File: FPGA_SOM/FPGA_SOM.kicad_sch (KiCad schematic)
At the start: 88 parts, among them J1 Conn_01x02, J1 USB_C_Receptacle_USB2.0, J3 Conn_02x06_Top_Bottom, J4 Conn_02x04_Counter_Clockwise, J5 Conn_01x06, J6 Conn_01x06, SW1 SW_Push, SW2 SW_Push, SW3 SW_Push, U101 W25Q128JVSIQ, U2 ICE40UP5K-SG48ITR, U3 AP2127N-3.3, U4 AP2127N-1.2, X101 SX2M36.000B10F20TNN

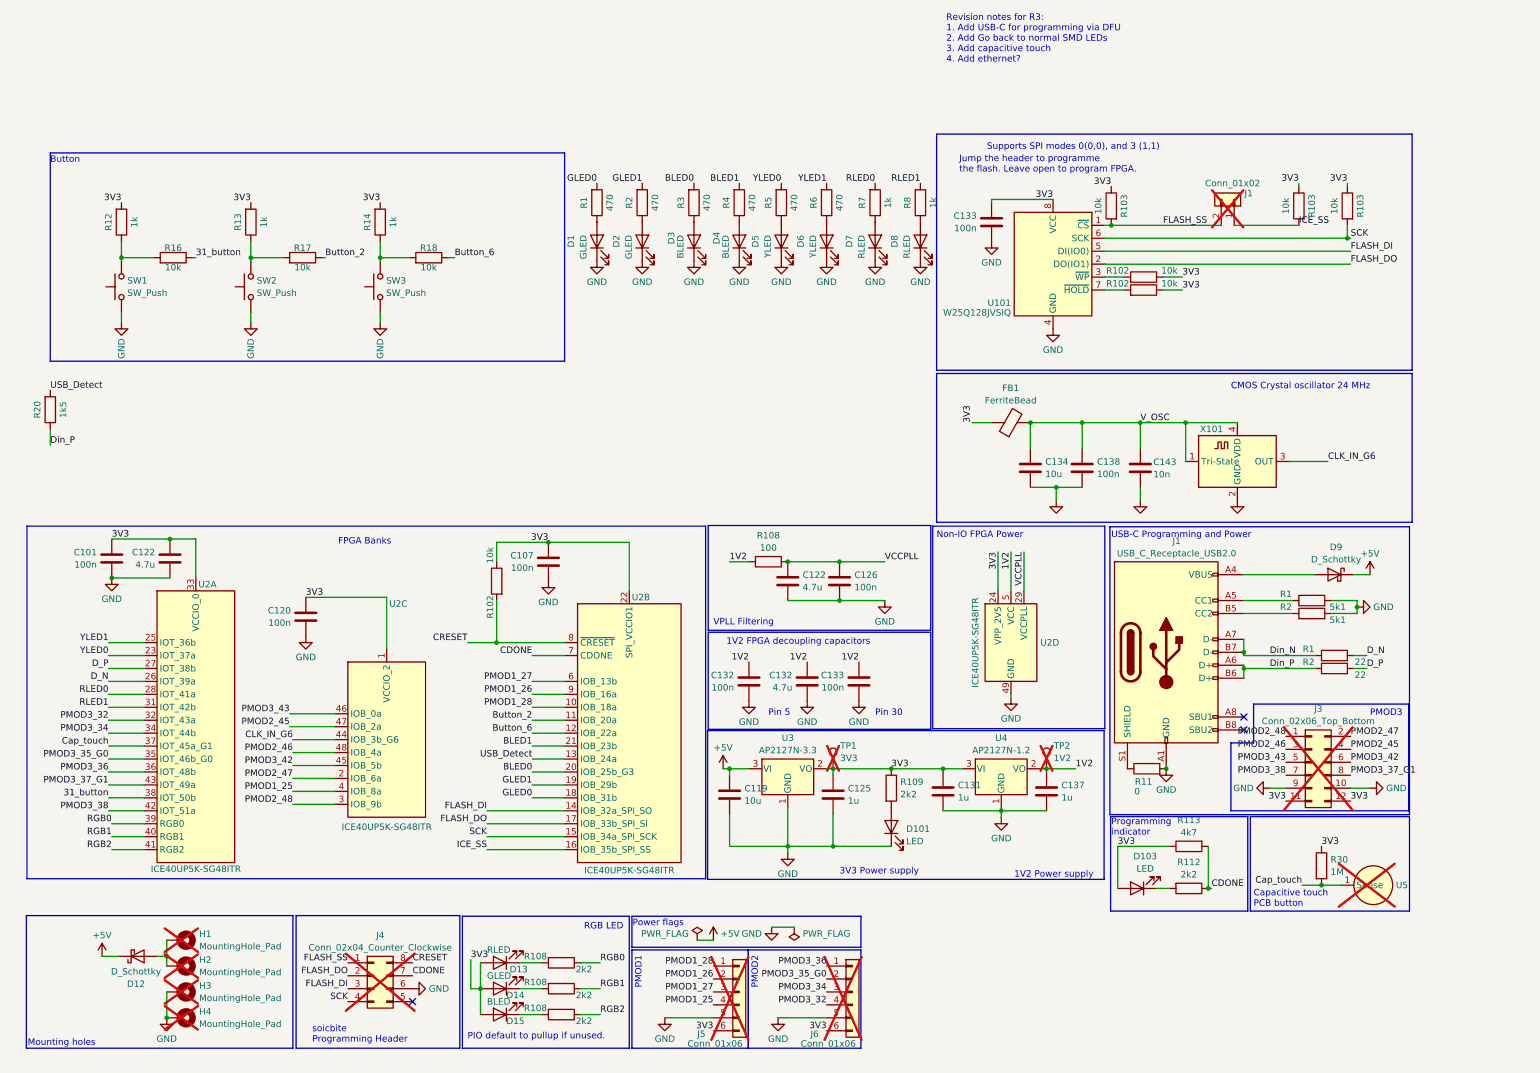
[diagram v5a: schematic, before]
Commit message: Kicad Update changes some things. Also reorganise nets.
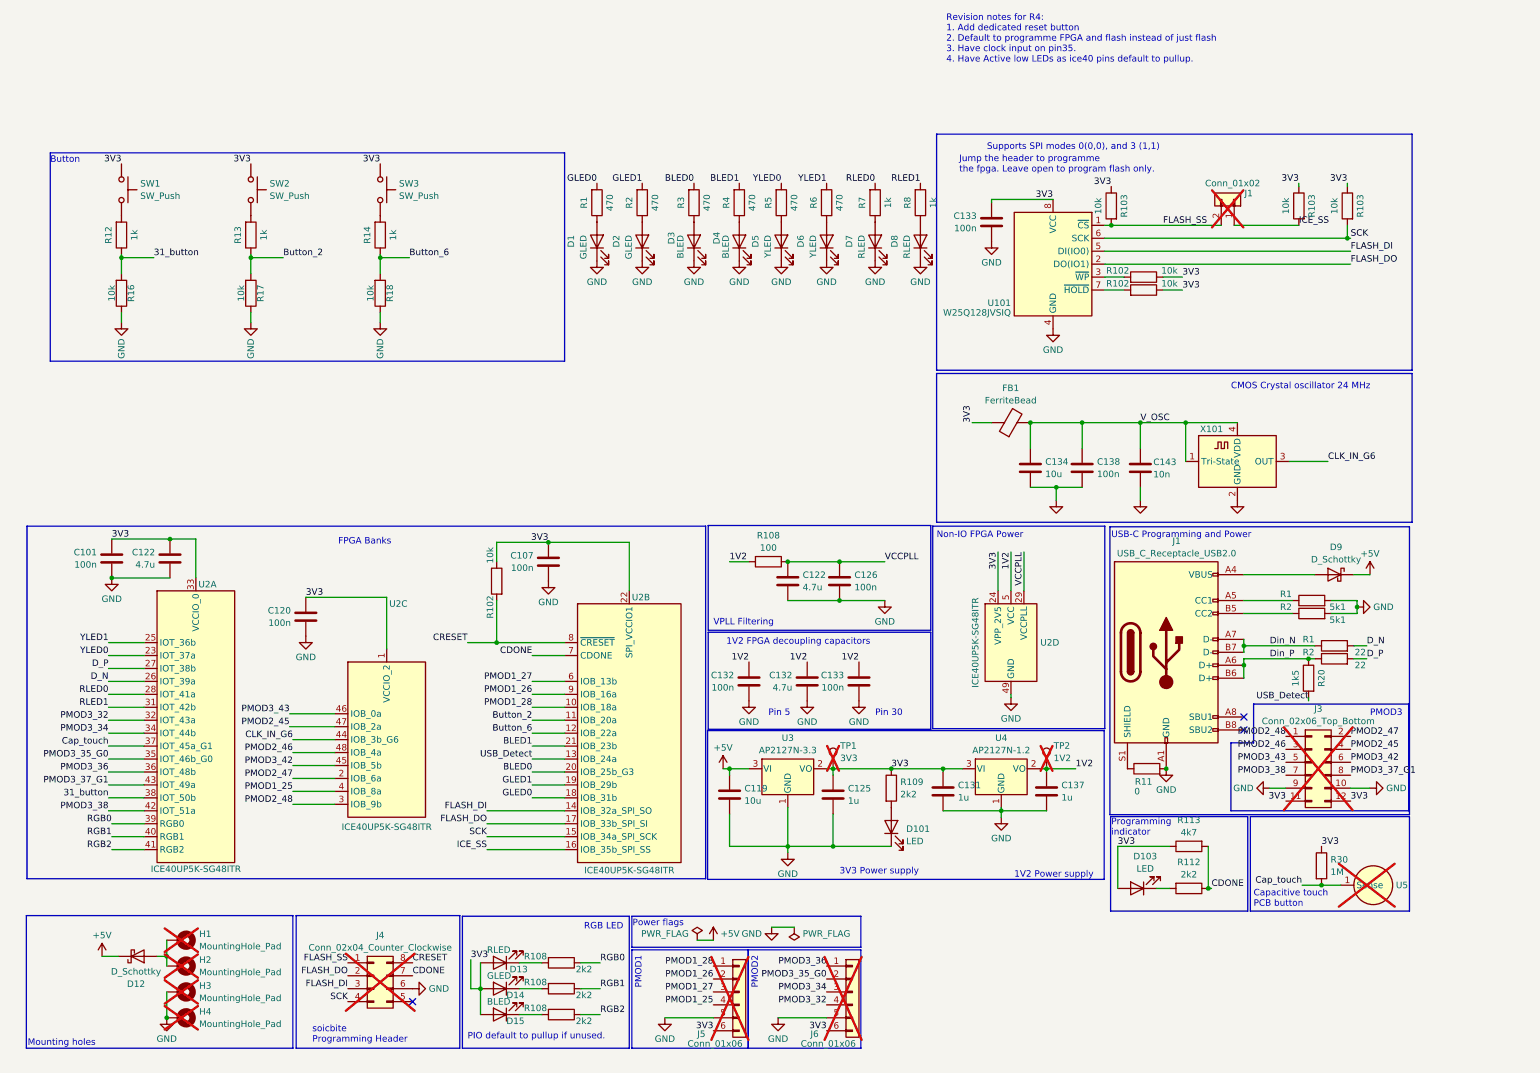
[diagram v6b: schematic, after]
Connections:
- net 31_button: now also R12.1, R16.2; no longer R16.1
- net 3V3: now also SW1.1, SW2.1, SW3.1; no longer R12.2, R13.2, R14.2
- net Button_2: now also R13.1, R17.2; no longer R17.1
- net Button_6: now also R14.1, R18.2; no longer R18.1
- net GND: now also R16.1, R17.1, R18.1; no longer SW1.1, SW2.1, SW3.1
- new net: R13.2, SW2.2
- new net: R12.2, SW1.2
- new net: R14.2, SW3.2
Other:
- note added: "Jump the header to programme the fpga. Leave open to program flash only."
- note added: "Revision notes for R4: 1. Add dedicated reset button 2. Default to programme FPGA and flash instead of just flash 3. Have clock input on pin35. 4. Have Active low LEDs as ice40 pins default to pullup."
- note removed: "Jump the header to programme the flash. Leave open to program FPGA."
- note removed: "Revision notes for R3: 1. Add USB-C for programming via DFU 2. Add Go back to normal SMD LEDs 3. Add capacitive touch 4. Add ethernet?"
- moved on the sheet: R1, R12, R13, R14, R16, R17, R18, R2, R20, SW1, SW2, SW3
